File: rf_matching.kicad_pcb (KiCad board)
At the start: 2 copper layers, 46.6 x 32.6 mm, 12 parts, among them J1 RFI, J2 RFO, J3 CTRL, J4 ANT, J5 3V3, U1 pe4259ds, U2 SF2098

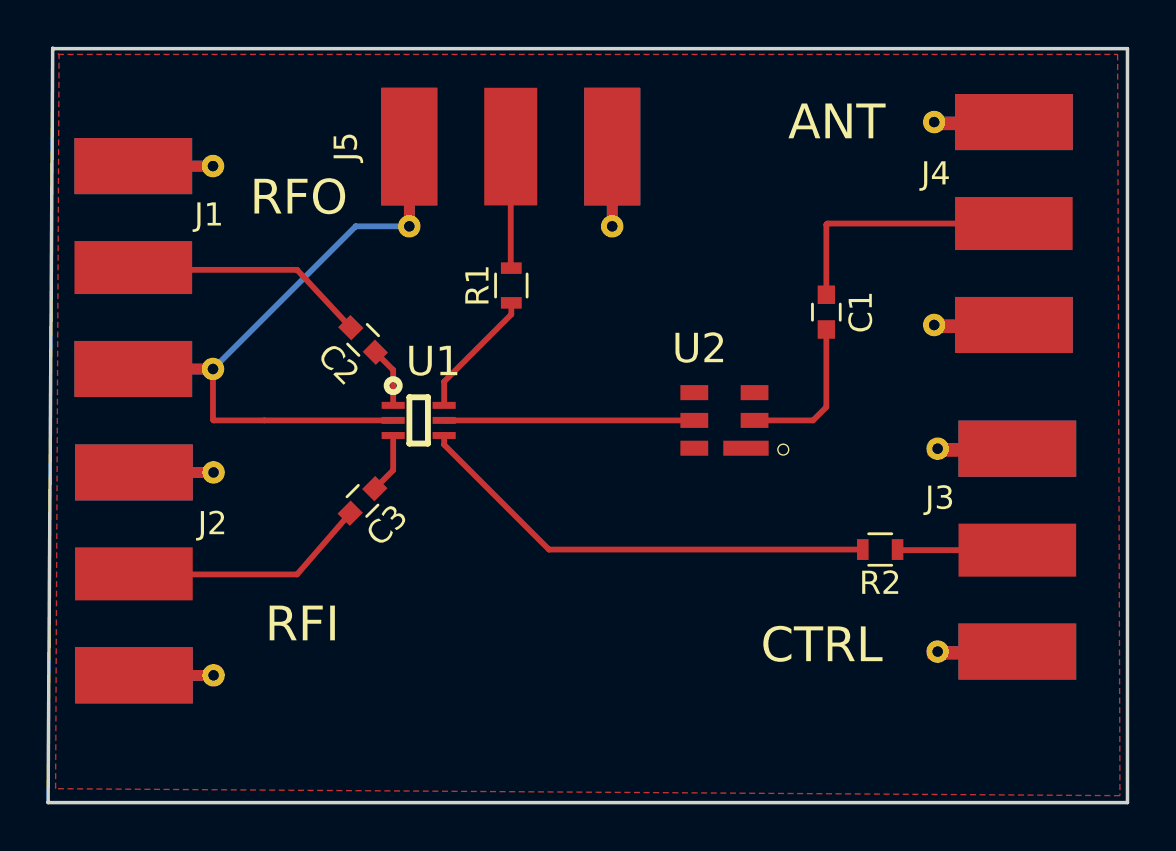
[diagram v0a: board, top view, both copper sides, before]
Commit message: Fixing ground plane dubiously through the connectors, sparing a link and going single layer... will it work/perform well?
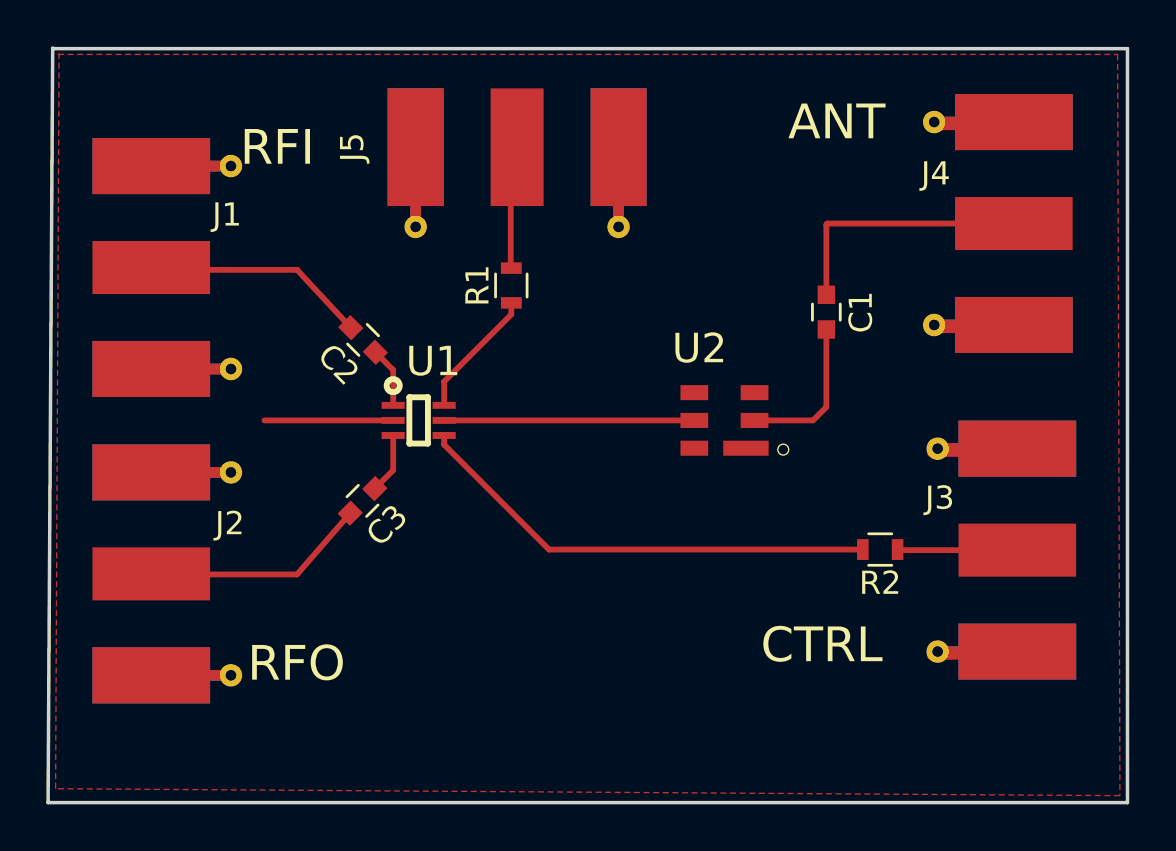
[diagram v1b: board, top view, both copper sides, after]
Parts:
- moved J1 0.78 mm to (160.1, 87.2)
- moved J2 0.75 mm to (160.1, 100.4)
- moved J5 0.28 mm to (174.1, 83.7)
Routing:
- net GND: track 55.4 -> 46.8 mm
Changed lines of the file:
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@@
   (thickness 1.6)
   (drawings 10)
-  (tracks 43)
+  (tracks 40)
   (zones 0)
   (modules 12)
@@
   (thickness 1.6)
   (drawings 10)
-  (tracks 43)
+  (tracks 40)
   (zones 0)
   (modules 12)
@@
 )
 (setup
-  (last_trace_width 0.25)
+  (last_trace_width 1)
   (user_trace_width 1)
   (trace_clearance 0.2)
@@
 )
   (module KiCad/Connectors_Molex.pretty:Molex_SMA_Jack_Edge_Mount (layer F.Cu)
-    (at 159.275 87.15)
+    (at 160.05 87.15)
     (descr "Molex SMA Jack, Edge Mount, http://www.molex.com/pdm_docs/sd/732511150_sd.pdf")
     (tags "sma edge")
@@
       (effects (font (size 1 1) (thickness 0.15)))
     )
-    (fp_text value RFI (at 3.8 -7.3) (layer F.Fab)
+    (fp_text value RFI (at 4.1 -3.35) (layer F.Fab)
       (effects (font (size 1 1) (thickness 0.15)))
     )
@@
   )
   (module KiCad/Connectors_Molex.pretty:Molex_SMA_Jack_Edge_Mount (layer F.Cu)
-    (at 159.3 100.375)
+    (at 160.05 100.375)
     (descr "Molex SMA Jack, Edge Mount, http://www.molex.com/pdm_docs/sd/732511150_sd.pdf")
     (tags "sma edge")
@@
   )
   (module KiCad/Connectors_Molex.pretty:Molex_SMA_Jack_Edge_Mount (layer F.Cu)
-    (at 173.85 83.65 270)
+    (at 174.125 83.675 270)
     (descr "Molex SMA Jack, Edge Mount, http://www.molex.com/pdm_docs/sd/732511150_sd.pdf")
     (tags "sma edge")
@@
   )
   (target plus (at 153.9 110.225) (size 5) (width 0.15) (layer Edge.Cuts))
-  (gr_text RFI (at 164.85 102.55) (layer F.SilkS)
+  (gr_text RFI (at 163.775 81.975) (layer F.SilkS)
     (effects (font (size 1.5 1.5) (thickness 0.3)))
   )
-  (gr_text RFO (at 164.7 84.125) (layer F.SilkS)
+  (gr_text RFO (at 164.6 104.25) (layer F.SilkS)
     (effects (font (size 1.5 1.5) (thickness 0.3)))
   )
@@
   (gr_line (start 200.475 77.7) (end 200.475 110.25) (layer Edge.Cuts) (width 0.15))
   (gr_line (start 154.075 77.7) (end 200.475 77.7) (layer Edge.Cuts) (width 0.15))
-  (segment (start 160.995 93.72) (end 161.025 93.75) (width 0.25) (layer F.Cu) (net 1))
-  (segment (start 161.025 93.75) (end 163.215 93.75) (width 0.25) (layer F.Cu) (net 1))
-  (segment (start 160.995 91.53) (end 160.995 93.72) (width 0.25) (layer F.Cu) (net 1))
+  (segment (start 178.505 85.395) (end 178.505 81.955) (width 0.25) (layer F.Cu) (net 1))
+  (segment (start 169.745 85.395) (end 169.745 81.955) (width 0.25) (layer F.Cu) (net 1))
+  (segment (start 178.255 84.195) (end 178.255 80.755) (width 0.25) (layer F.Cu) (net 1))
+  (segment (start 169.495 84.195) (end 169.495 80.755) (width 0.25) (layer F.Cu) (net 1))
   (segment (start 168.775 93.75) (end 163.215 93.75) (width 0.25) (layer F.Cu) (net 1))
-  (segment (start 169.47 85.37) (end 167.155 85.37) (width 0.25) (layer B.Cu) (net 1))
-  (segment (start 167.155 85.37) (end 160.995 91.53) (width 0.25) (layer B.Cu) (net 1))
   (segment (start 157.58 95.995) (end 160.37 95.995) (width 0.25) (layer F.Cu) (net 1))
   (segment (start 160.37 95.995) (end 161.02 95.995) (width 0.25) (layer F.Cu) (net 1))
@@
   (segment (start 190.575 99.35) (end 190.55 99.325) (width 0.25) (layer F.Cu) (net 2))
   (segment (start 170.975 93.75) (end 181.775 93.75) (width 0.25) (layer F.Cu) (net 3))
+  (segment (start 173.85 81.93) (end 173.85 87.15) (width 0.25) (layer F.Cu) (net 4))
   (segment (start 170.975 93.1) (end 170.975 92.075) (width 0.25) (layer F.Cu) (net 5))
   (segment (start 170.975 92.075) (end 173.875 89.175) (width 0.25) (layer F.Cu) (net 5))
@@
   (segment (start 164.625 100.4) (end 157.68 100.4) (width 0.25) (layer F.Cu) (net 12))
   (segment (start 164.625 87.25) (end 157.655 87.25) (width 0.25) (layer F.Cu) (net 9))
-  (segment (start 169.47 81.93) (end 169.47 85.37) (width 0.25) (layer F.Cu) (net 1))
-  (segment (start 178.23 85.37) (end 178.23 81.93) (width 0.25) (layer F.Cu) (net 1))
   (segment (start 157.655 91.63) (end 161.095 91.63) (width 0.25) (layer F.Cu) (net 1))
   (segment (start 157.655 82.87) (end 161.095 82.87) (width 0.25) (layer F.Cu) (net 1))
@@
   (segment (start 195.395 95.195) (end 191.955 95.195) (width 0.25) (layer F.Cu) (net 1))
   (segment (start 195.395 103.955) (end 191.955 103.955) (width 0.25) (layer F.Cu) (net 1))
-  (segment (start 173.85 81.93) (end 173.85 87.15) (width 0.25) (layer F.Cu) (net 4))
   (segment (start 173.85 87.15) (end 173.875 87.175) (width 0.25) (layer F.Cu) (net 4))
   (segment (start 187.475 88.325) (end 187.475 85.3) (width 0.25) (layer F.Cu) (net 8))

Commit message: RF switch only branch
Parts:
- removed U2: SF2098, SON120P300X300X110-6N:SON120P300X300X110-6N
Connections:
- U1 pad 5: Net-(U1-Pad5) -> Net-(C1-Pad2)
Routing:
- net Net-(C1-Pad2): track 6.69 -> 20.3 mm
- net Net-(U1-Pad5): track 10.8 -> 0.00 mm
